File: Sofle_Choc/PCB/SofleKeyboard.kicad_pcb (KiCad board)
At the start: 2 copper layers, 143.4 x 111.8 mm, 84 parts, among them J2 4PIN, J3 OLED, P1 i2c_pin, P2 i2c_pin, SW1 SW_PUSH_LED, SW10 SW_PUSH_LED, SW11 SW_PUSH_LED, SW12 SW_PUSH_LED, SW13 SW_PUSH_LED, SW14 SW_PUSH_LED, SW15 SW_PUSH_LED, SW16 SW_PUSH_LED, SW17 SW_PUSH_LED, SW18 SW_PUSH_LED, SW19 SW_PUSH_LED, SW2 SW_PUSH_LED, SW20 SW_PUSH_LED, SW21 SW_PUSH_LED, SW22 SW_PUSH_LED, SW23 SW_PUSH_LED, SW24 SW_PUSH_LED, SW25 Rotary_Encoder_Switch, SW26 SW_PUSH_LED, SW27 SW_PUSH_LED, SW28 SW_PUSH_LED, SW29 SW_PUSH_LED, SW3 SW_PUSH_LED, SW30 SW_PUSH_LED, SW4 SW_PUSH_LED, SW5 SW_PUSH_LED, SW6 SW_PUSH_LED, SW7 SW_PUSH_LED, SW8 SW_PUSH_LED, SW9 SW_PUSH_LED, U1 ProMicro

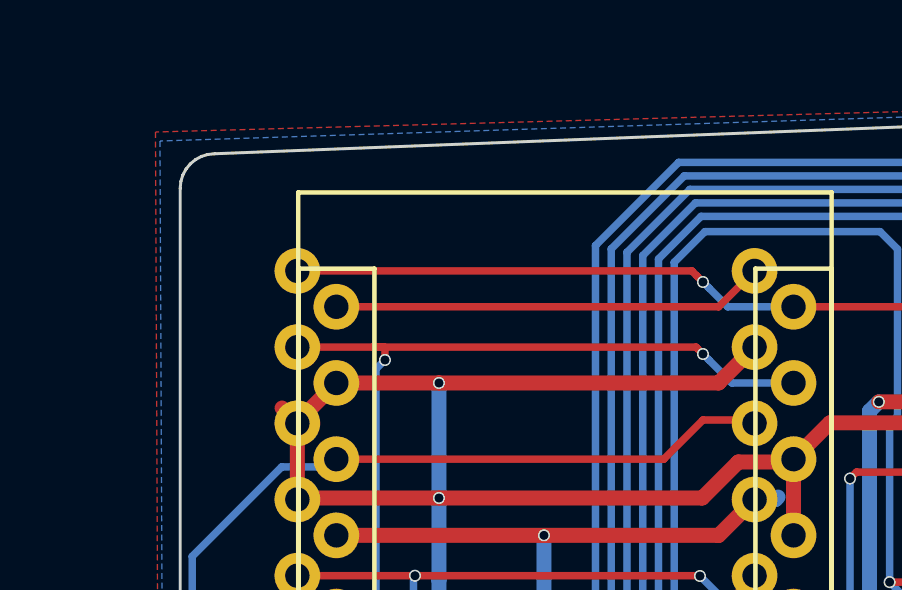
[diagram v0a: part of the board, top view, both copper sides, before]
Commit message: Add power switch and battery tht pads to Sofle Choc
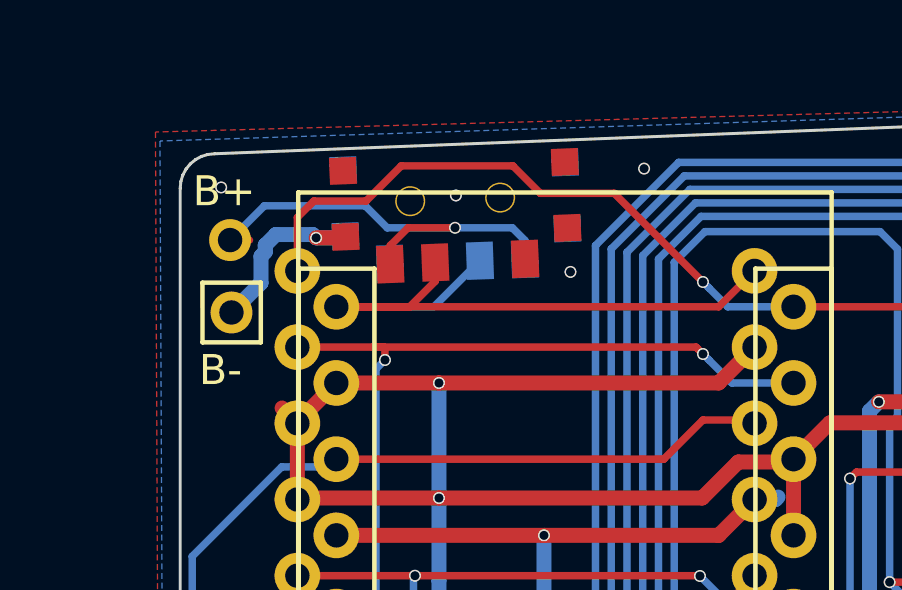
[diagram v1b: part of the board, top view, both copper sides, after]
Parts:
- added Bat_+1: MountingHole, MountingHole:MountingHole_2.1mm, F.Cu at (89.9, 40.2)
- added Bat_-1: MountingHole, MountingHole:MountingHole_2.1mm, F.Cu at (90.0, 42.6)
- added Power_SW1: SW_SPDT, SofleChoc:SPDT_C128955, F.Cu at (97.4, 38.8)
- added Power_SW_R1: SW_SPDT, SofleChoc:SPDT_C128955r, B.Cu at (97.4, 38.8)
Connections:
- U1 pad 24: Net-(U1-Pad24) -> RAW
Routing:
- net RAW: track 0.00 -> 24.2 mm
- net Bat+: track 0.00 -> 15.1 mm, vias 0 -> 1
- net Net-(U1-Pad24): track 14.4 -> 0.00 mm
- net GND: track 1090.4 -> 1097.0 mm, vias 43 -> 48
- net LED: track 37.3 -> 41.2 mm
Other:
- board text added: "B+"
- board text added: "B-"

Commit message: Minimum to meet AllPcb freebie size
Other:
- board size 143.4 x 111.8 mm -> 138 x 108.2 mm
